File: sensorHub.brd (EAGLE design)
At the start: 70 x 70 mm, 12 parts

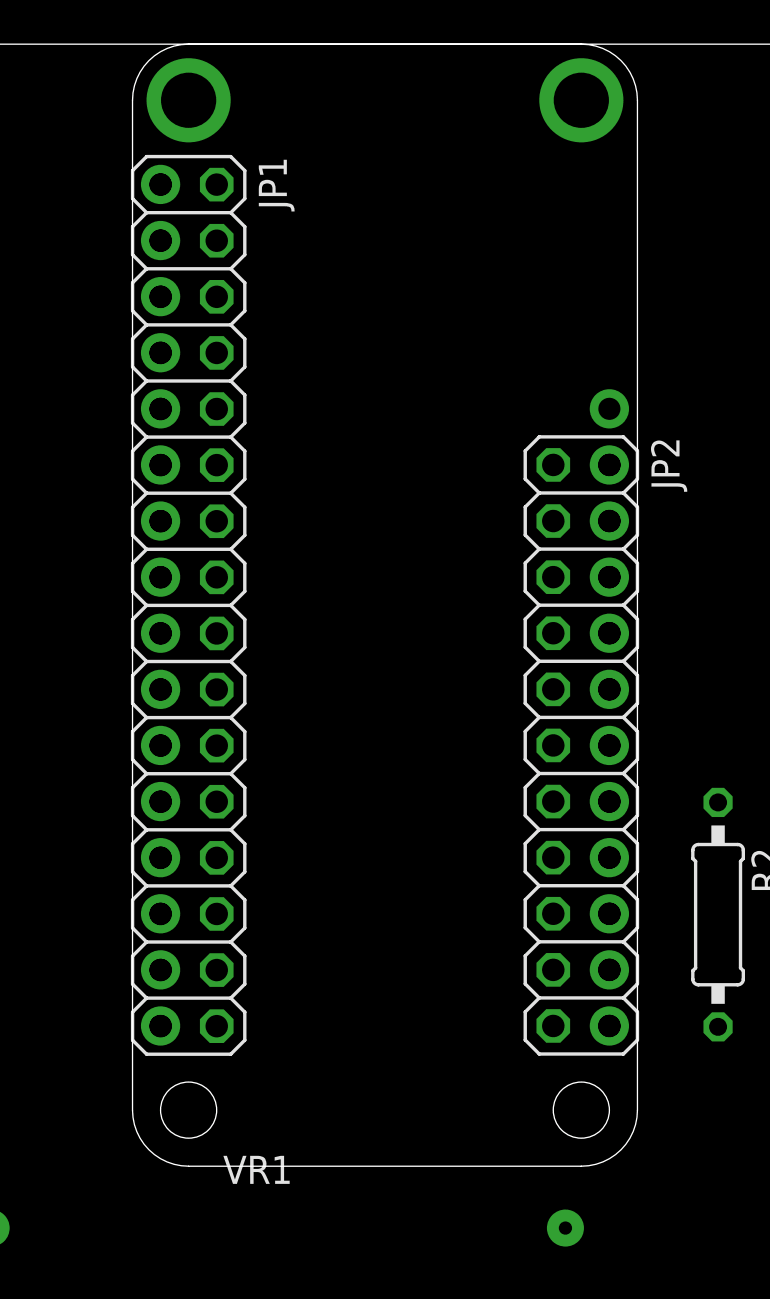
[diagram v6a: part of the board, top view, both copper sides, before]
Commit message: Deletes the feather board
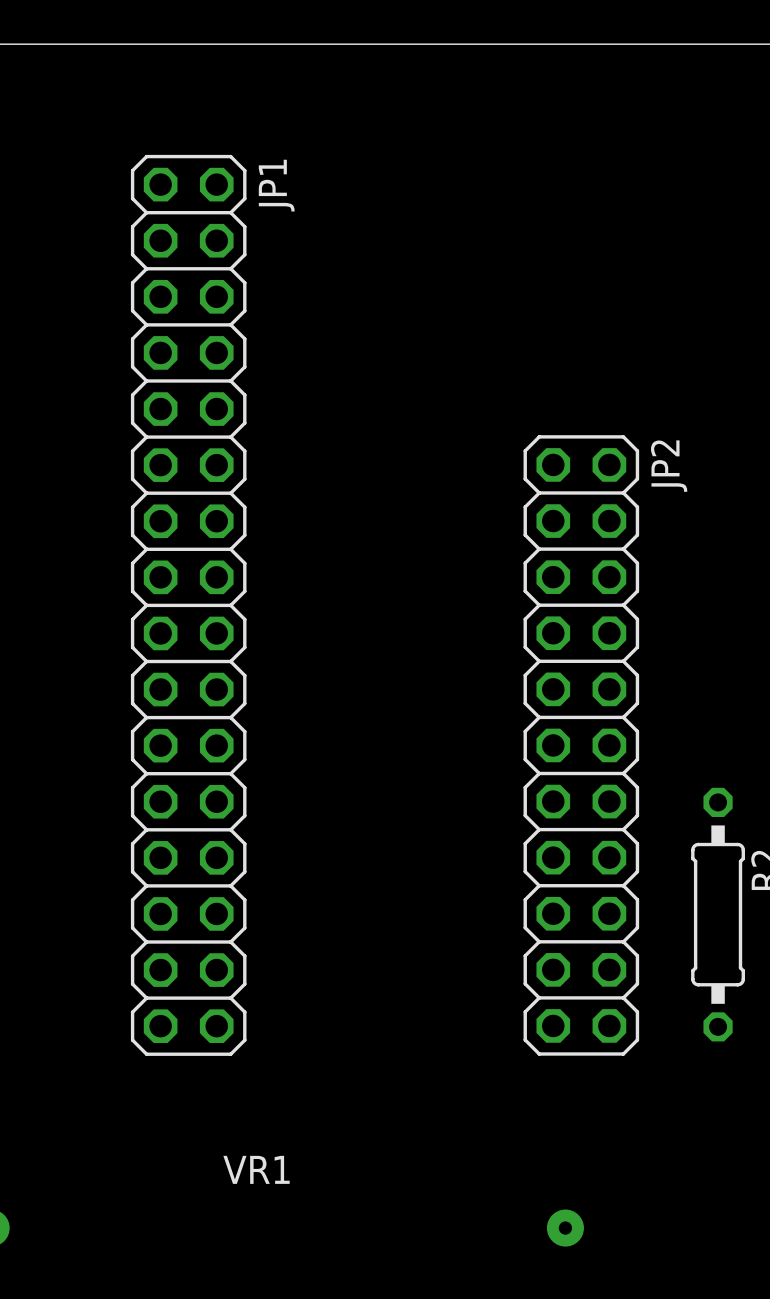
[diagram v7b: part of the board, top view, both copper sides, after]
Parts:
- removed MS1: FEATHERWING, adafruit:FEATHERWING
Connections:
- net GND: no longer MS1.4
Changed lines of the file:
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@@
 </autorouter>
 <elements>
-<element name="MS1" library="adafruit" package="FEATHERWING" value="FEATHERWING" x="35" y="70" locked="yes" smashed="yes" rot="R270"/>
 <element name="JP1" library="pinhead" library_urn="urn:adsk.eagle:library:325" package="2X16" package3d_urn="urn:adsk.eagle:package:22431/2" value="" x="37.543" y="44.591" locked="yes" smashed="yes" rot="R270">
 <attribute name="NAME" x="40.718" y="64.911" locked="yes" size="1.27" layer="25" ratio="10" rot="R270"/>
@@
 <signals>
 <signal name="GND">
-<contactref element="MS1" pad="4"/>
 <contactref element="JP1" pad="7"/>
 <contactref element="JP1" pad="8"/>
@@
 <contactref element="SHT10" pad="2"/>
 <contactref element="C02" pad="1"/>
-<wire x1="36.27" y1="56.03" x2="38.813" y2="56.021" width="0" layer="19" extent="1-1"/>
-<wire x1="36.273" y1="56.021" x2="36.27" y2="56.03" width="0" layer="19" extent="1-1"/>
-<wire x1="17.62" y1="57.43" x2="36.27" y2="56.03" width="0" layer="19" extent="1-1"/>
+<wire x1="36.273" y1="56.021" x2="38.813" y2="56.021" width="0" layer="19" extent="1-1"/>
+<wire x1="17.62" y1="57.43" x2="36.273" y2="56.021" width="0" layer="19" extent="1-1"/>
 <wire x1="3.49" y1="57.39" x2="17.62" y2="57.43" width="0" layer="19" extent="1-1"/>
-<wire x1="3.7" y1="6.79" x2="3.49" y2="57.39" width="0" layer="19" extent="1-1"/>
-<wire x1="3.52" y1="45.19" x2="3.7" y2="6.79" width="0" layer="19" extent="1-1"/>
+<wire x1="3.52" y1="45.19" x2="3.49" y2="57.39" width="0" layer="19" extent="1-1"/>
 <wire x1="3.36" y1="31.44" x2="3.52" y2="45.19" width="0" layer="19" extent="1-1"/>
-<wire x1="28.6" y1="16.4" x2="3.36" y2="31.44" width="0" layer="19" extent="1-1"/>
+<wire x1="3.7" y1="6.79" x2="3.36" y2="31.44" width="0" layer="19" extent="1-1"/>
+<wire x1="28.6" y1="16.4" x2="3.7" y2="6.79" width="0" layer="19" extent="1-1"/>
 <wire x1="54.6" y1="16.4" x2="28.6" y2="16.4" width="0" layer="19" extent="1-1"/>
 </signal>

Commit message: Completes the brd file
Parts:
- moved R1 21.3 mm to (49.2, 19.7), turned to 0 degrees
- moved R2 12.7 mm to (51.4, 22.8), turned to 0 degrees
- moved VBAT 4.88 mm to (65.7, 3.30), turned to 90 degrees
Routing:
- net 3V: track 0.00 -> 151.2 mm
- net SCL: track 0.00 -> 120.6 mm, vias 0 -> 2
- net SDA: track 0.00 -> 117.2 mm
- net D5: track 0.00 -> 63.8 mm, vias 0 -> 2
- net GND: track 0.00 -> 48.5 mm, vias 0 -> 4
- net RX: track 0.00 -> 43.9 mm
- net TX: track 0.00 -> 43.2 mm
- net A2: track 0.00 -> 38.3 mm, vias 0 -> 2
- net 5V: track 0.00 -> 28.2 mm
- net VBAT: track 0.00 -> 14.0 mm
- net N$24: track 0.00 -> 2.54 mm
- net N$23: track 0.00 -> 2.54 mm
- net N$22: track 0.00 -> 2.54 mm
- net N$21: track 0.00 -> 2.54 mm
- net N$20: track 0.00 -> 2.54 mm
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- added copper zone on layer 1, net GND
- added copper zone on layer 16, net GND
